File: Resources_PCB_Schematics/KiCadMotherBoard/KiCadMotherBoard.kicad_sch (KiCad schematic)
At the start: 21 parts, among them J10 Conn_01x02_Male_DATA, J11 Conn_01x02_Male_DATA, J12 Conn_01x02_Male_DATA, J13 Conn_01x02_Male_DATA, J15 Conn_01x02_Male_DATA, J16 Conn_01x02_Male_DATA, J2 Conn_01x02_Male, J3 Conn_01x02_Male, J4 Conn_01x02_Male, J5 Conn_01x02_Male, J6 Conn_01x02_Male, J7 Conn_01x02_Male, J8 Conn_01x02_Male, J9 Conn_01x02_Male_DATA

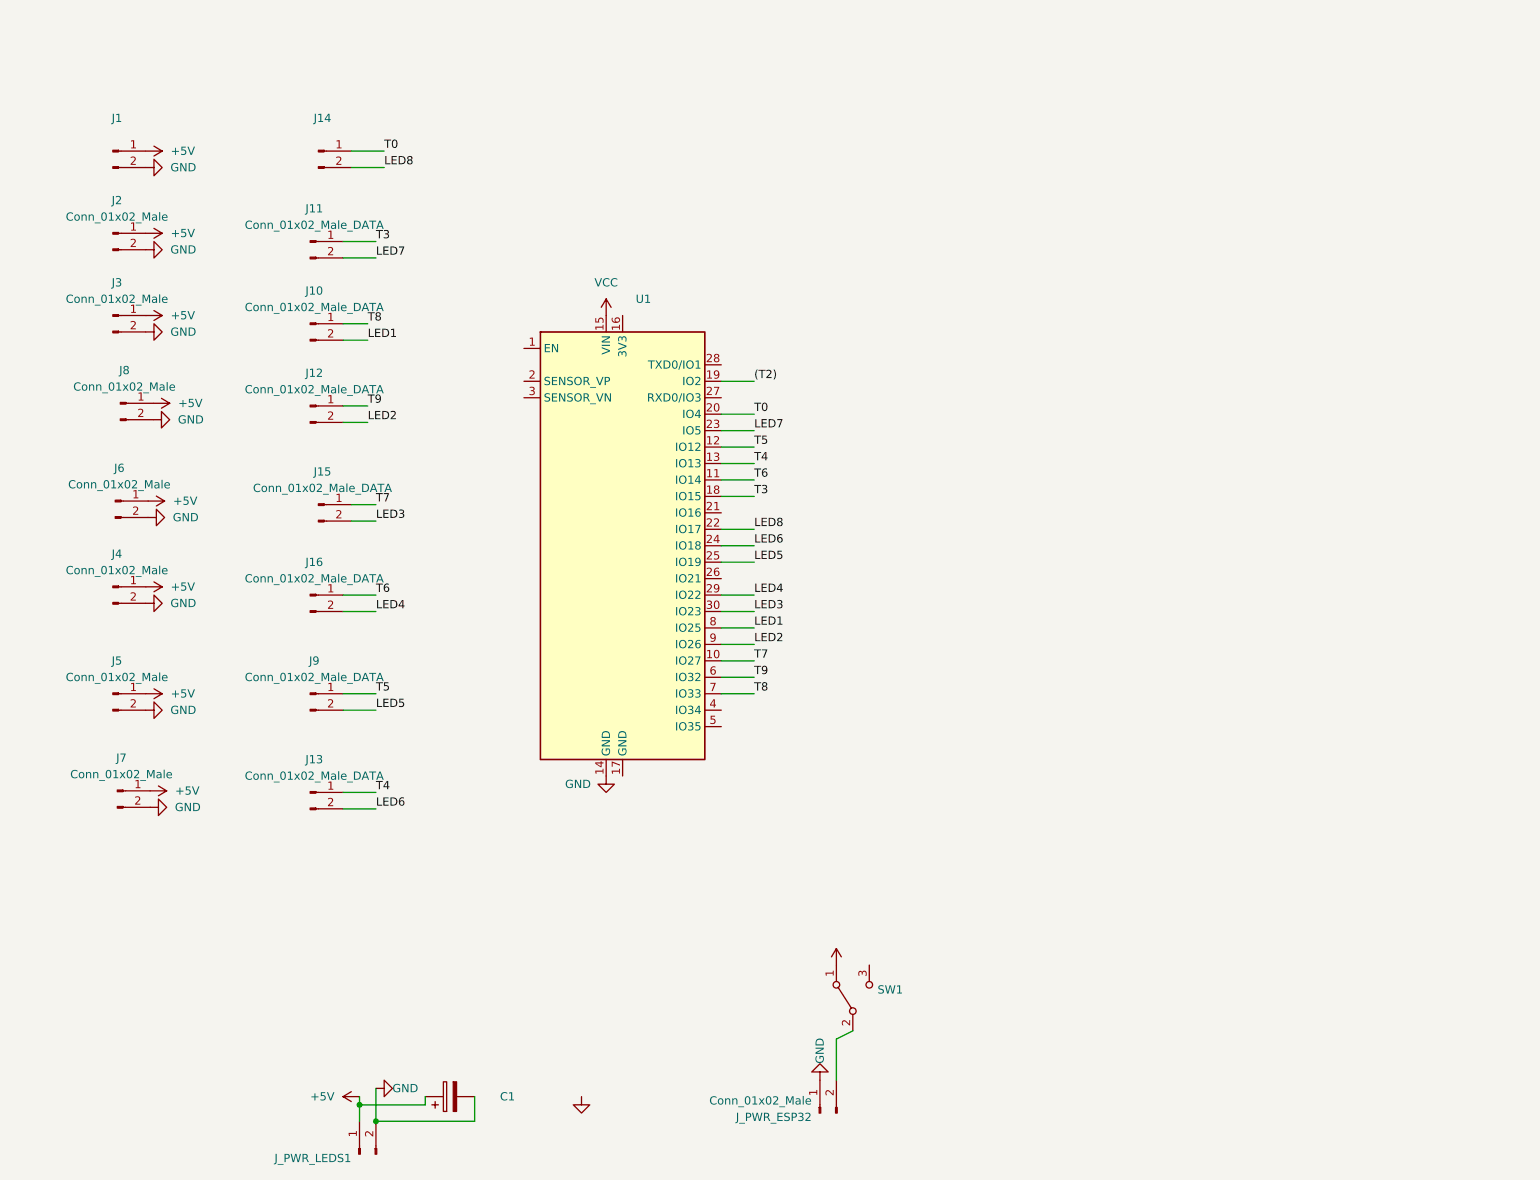
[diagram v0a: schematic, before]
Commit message: Moved to adafruit Neopixel Library, more tests to do. Fast led don't work
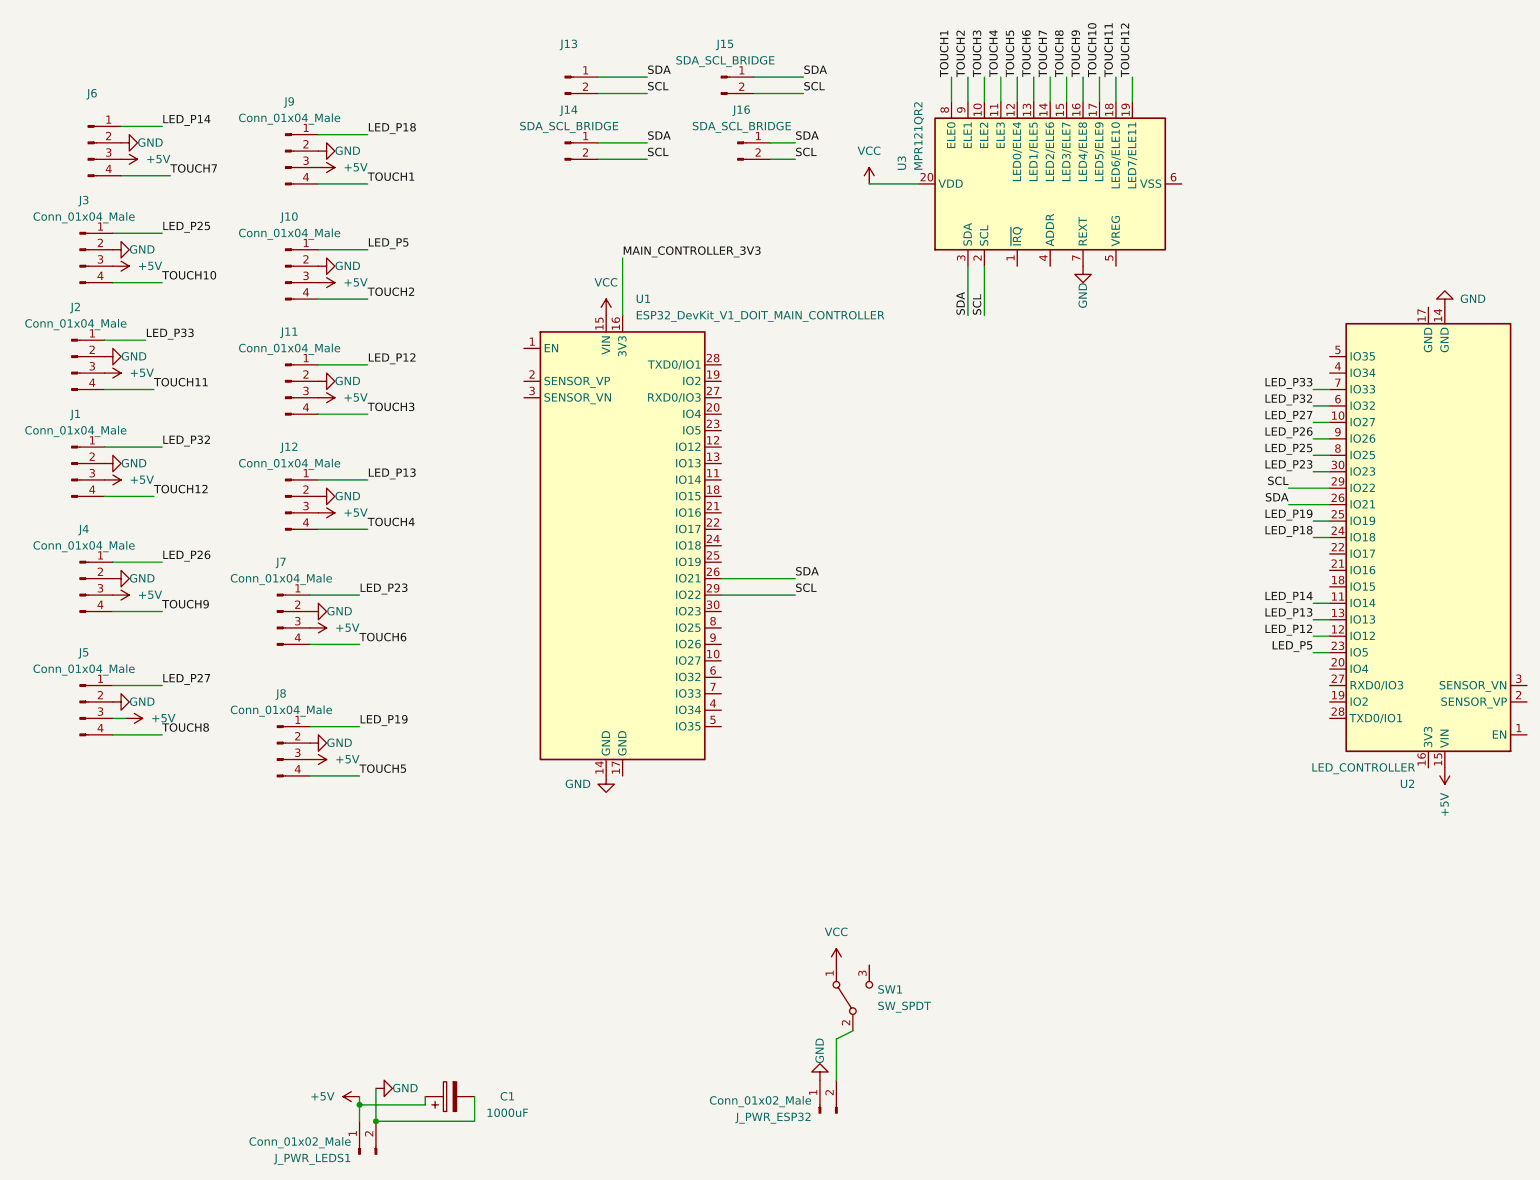
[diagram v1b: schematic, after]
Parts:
- removed J1: (no value), symbol Connector:Conn_01x02_Male
- removed J10, J11, J12, J9: Conn_01x02_Male_DATA, Connector_JST:JST_XH_B2B-XH-A_1x02_P2.50mm_Vertical, symbol Connector:Conn_01x02_Male
- removed J2, J3, J4, J5, J6, J7, J8: Conn_01x02_Male, Connector_JST:JST_XH_B2B-XH-A_1x02_P2.50mm_Vertical, symbol Connector:Conn_01x02_Male
- added J1, J10, J11, J12, J2, J3, J4, J5, J7, J8, J9: Conn_01x04_Male, symbol Connector:Conn_01x04_Male
- added J6: (no value), symbol Connector:Conn_01x04_Male
- added U2: LED_CONTROLLER, ESP32_devkit_v1:esp32_devkit_v1_doit, symbol ESP32_devkit_v1:ESP32_DevKit_V1_DOIT
- added U3: MPR121QR2, symbol Sensor_Touch:MPR121QR2
- C1: value (none) -> 1000uF; footprint (none) -> Capacitor_THT:CP_Radial_D10.0mm_P5.00mm
- J13: value Conn_01x02_Male_DATA -> (none); footprint Connector_JST:JST_XH_B2B-XH-A_1x02_P2.50mm_Vertical -> (none)
- J14: value (none) -> SDA_SCL_BRIDGE; footprint Connector_JST:JST_XH_B2B-XH-A_1x02_P2.50mm_Vertical -> (none)
- J15: value Conn_01x02_Male_DATA -> SDA_SCL_BRIDGE; footprint Connector_JST:JST_XH_B2B-XH-A_1x02_P2.50mm_Vertical -> (none)
- J16: value Conn_01x02_Male_DATA -> SDA_SCL_BRIDGE; footprint Connector_JST:JST_XH_B2B-XH-A_1x02_P2.50mm_Vertical -> Connector_JST:JST_XH_B2B-XH-AM_1x02_P2.50mm_Vertical
- J_PWR_LEDS1: value (none) -> Conn_01x02_Male; footprint (none) -> Connector_JST:JST_XH_B2B-XH-A_1x02_P2.50mm_Vertical
- SW1: value (none) -> SW_SPDT; footprint (none) -> Button_Switch_SMD:SW_DPDT_CK_JS202011JCQN
- U1: value (none) -> ESP32_DevKit_V1_DOIT_MAIN_CONTROLLER; footprint (none) -> ESP32_devkit_v1:esp32_devkit_v1_doit
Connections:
- net +5V: now also J1.3 (Pin_3), J10.3 (Pin_3), J11.3 (Pin_3), J12.3 (Pin_3), J2.3 (Pin_3), J3.3 (Pin_3), J4.3 (Pin_3), J5.3 (Pin_3), J6.3 (Pin_3), J7.3 (Pin_3), J8.3 (Pin_3), J9.3 (Pin_3), U2.15 (VIN)
- net GND: now also J1.2 (Pin_2), J10.2 (Pin_2), J11.2 (Pin_2), J12.2 (Pin_2), J2.2 (Pin_2), J3.2 (Pin_2), J4.2 (Pin_2), J5.2 (Pin_2), J6.2 (Pin_2), J7.2 (Pin_2), J8.2 (Pin_2), J9.2 (Pin_2), U2.14 (GND), U3.7 (REXT)
- net VCC: now also U3.20 (VDD)
- net MAIN_CONTROLLER_3V3: now reaches U1.16 (3V3)
- net SDA: now reaches U1.26 (IO21)
- net SDA: now also J13.1 (Pin_1), J14.1 (Pin_1), J15.1 (Pin_1), J16.1 (Pin_1), U2.26 (IO21), U3.3 (SDA)
- net (T2): no longer names the net of U1.19 (IO2)
- net LED1: no longer names the net of U1.8 (IO25)
- net LED2: no longer names the net of U1.9 (IO26)
- net LED3: no longer names the net of U1.30 (IO23)
- net LED3: no longer J15.2 (Pin_2)
- net LED4 renamed SCL
- net SCL: now also J13.2 (Pin_2), J14.2 (Pin_2), J15.2 (Pin_2), U2.29 (IO22), U3.2 (SCL)
- net LED5: no longer names the net of U1.25 (IO19)
- net LED6: no longer names the net of U1.24 (IO18)
- net LED6: no longer J13.2 (Pin_2)
- net LED7: no longer names the net of U1.23 (IO5)
- net LED8: no longer names the net of U1.22 (IO17)
- net LED8: no longer J14.2 (Pin_2)
- net T0: no longer names the net of U1.20 (IO4)
- net T0: no longer J14.1 (Pin_1)
- net T3: no longer names the net of U1.18 (IO15)
- net T4: no longer names the net of U1.13 (IO13)
- net T4: no longer J13.1 (Pin_1)
- net T5: no longer names the net of U1.12 (IO12)
- net T6: no longer names the net of U1.11 (IO14)
- net T6: no longer J16.1 (Pin_1)
- net T7: no longer names the net of U1.10 (IO27)
- net T7: no longer J15.1 (Pin_1)
- net T8: no longer names the net of U1.7 (IO33)
- net T9: no longer names the net of U1.6 (IO32)
- new net LED_P12: J11.1 (Pin_1), U2.12 (IO12)
- new net LED_P13: J12.1 (Pin_1), U2.13 (IO13)
- new net LED_P14: J6.1 (Pin_1), U2.11 (IO14)
- new net LED_P18: J9.1 (Pin_1), U2.24 (IO18)
- new net LED_P19: J8.1 (Pin_1), U2.25 (IO19)
- new net LED_P23: J7.1 (Pin_1), U2.30 (IO23)
- new net LED_P25: J3.1 (Pin_1), U2.8 (IO25)
- new net LED_P26: J4.1 (Pin_1), U2.9 (IO26)
- new net LED_P27: J5.1 (Pin_1), U2.10 (IO27)
- new net LED_P32: J1.1 (Pin_1), U2.6 (IO32)
- new net LED_P33: J2.1 (Pin_1), U2.7 (IO33)
- new net LED_P5: J10.1 (Pin_1), U2.23 (IO5)
- new net TOUCH1: J9.4 (Pin_4), U3.8 (ELE0)
- new net TOUCH10: J3.4 (Pin_4), U3.17 (LED5/ELE9)
- new net TOUCH11: J2.4 (Pin_4), U3.18 (LED6/ELE10)
- new net TOUCH12: J1.4 (Pin_4), U3.19 (LED7/ELE11)
- new net TOUCH2: J10.4 (Pin_4), U3.9 (ELE1)
- new net TOUCH3: J11.4 (Pin_4), U3.10 (ELE2)
- new net TOUCH4: J12.4 (Pin_4), U3.11 (ELE3)
- new net TOUCH5: J8.4 (Pin_4), U3.12 (LED0/ELE4)
- new net TOUCH6: J7.4 (Pin_4), U3.13 (LED1/ELE5)
- new net TOUCH7: J6.4 (Pin_4), U3.14 (LED2/ELE6)
- new net TOUCH8: J5.4 (Pin_4), U3.15 (LED3/ELE7)
- new net TOUCH9: J4.4 (Pin_4), U3.16 (LED4/ELE8)
